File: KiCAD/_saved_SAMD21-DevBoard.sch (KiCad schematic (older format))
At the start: 23 parts, among them J1 .1\" Headers, J2 .1\" Headers, J3 Cortex_Debug, SW1 B3FS-4005P, U1 SAMD21G18A-AU, Y1 32.768KHz

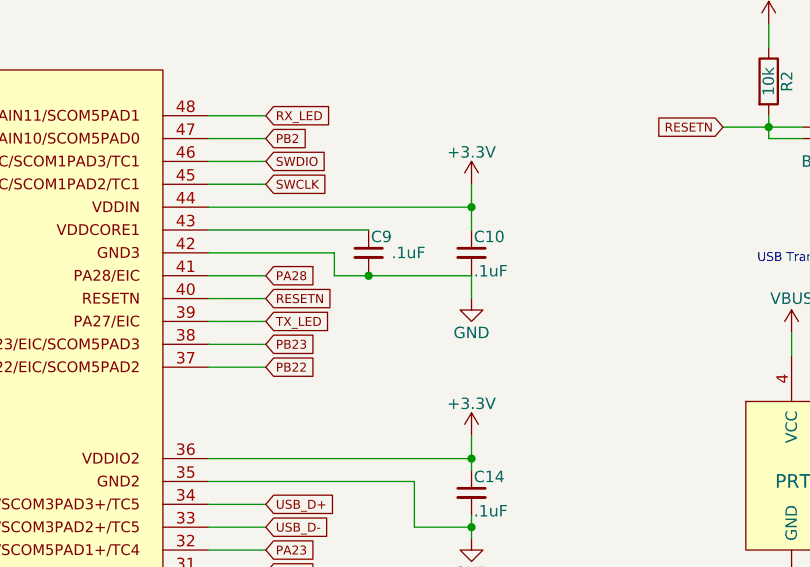
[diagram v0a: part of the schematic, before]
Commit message: Board layout and fixing schematic errors
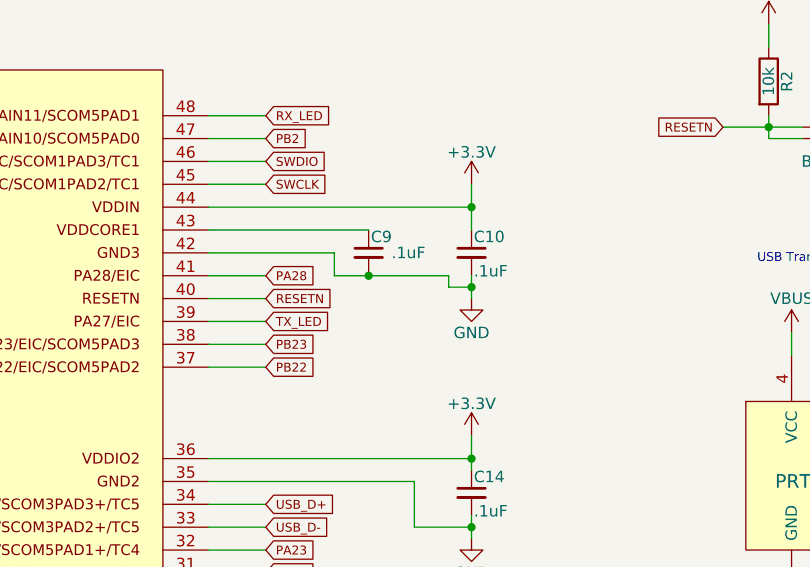
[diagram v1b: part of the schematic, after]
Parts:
- C14: footprint (none) -> Capacitors_SMD:C_1206
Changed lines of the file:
@@
 	6650 2400 6650 2500
-Wire Wire Line
-	6650 2500 7250 2500
 Wire Wire Line
 	7250 2300 7250 2100
@@
 	6100 2200 7250 2200
 Connection ~ 7250 2200
-Connection ~ 6800 2500
 $Comp
 L GND #PWR023
@@
 F 0 "C14" H 7260 3520 50  0000 L CNN
 F 1 ".1uF" H 7260 3370 50  0000 L CNN
-F 2 "" H 7250 3450 50  0001 C CNN
+F 2 "Capacitors_SMD:C_1206" H 7250 3450 50  0001 C CNN
 F 3 "" H 7250 3450 50  0001 C CNN
 	1    7250 3450
@@
 Connection ~ 7250 3600
 Connection ~ 7250 3300
+Wire Wire Line
+	6650 2500 7150 2500
+Wire Wire Line
+	7150 2500 7150 2550
+Wire Wire Line
+	7150 2550 7250 2550
+Connection ~ 7250 2550
+Connection ~ 6800 2500
 $EndSCHEMATC
